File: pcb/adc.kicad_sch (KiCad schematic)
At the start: 19 parts, among them U2 PCM1802DB, X1 ECS-2520MVLC-081.92

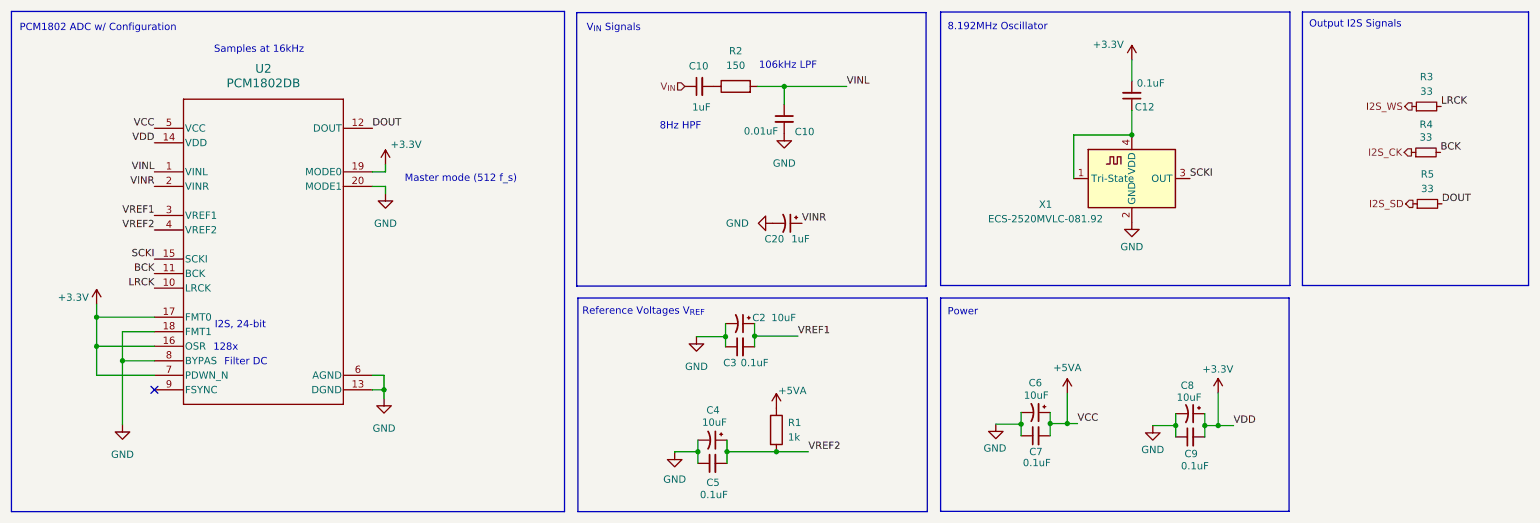
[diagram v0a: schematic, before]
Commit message: Reordered components
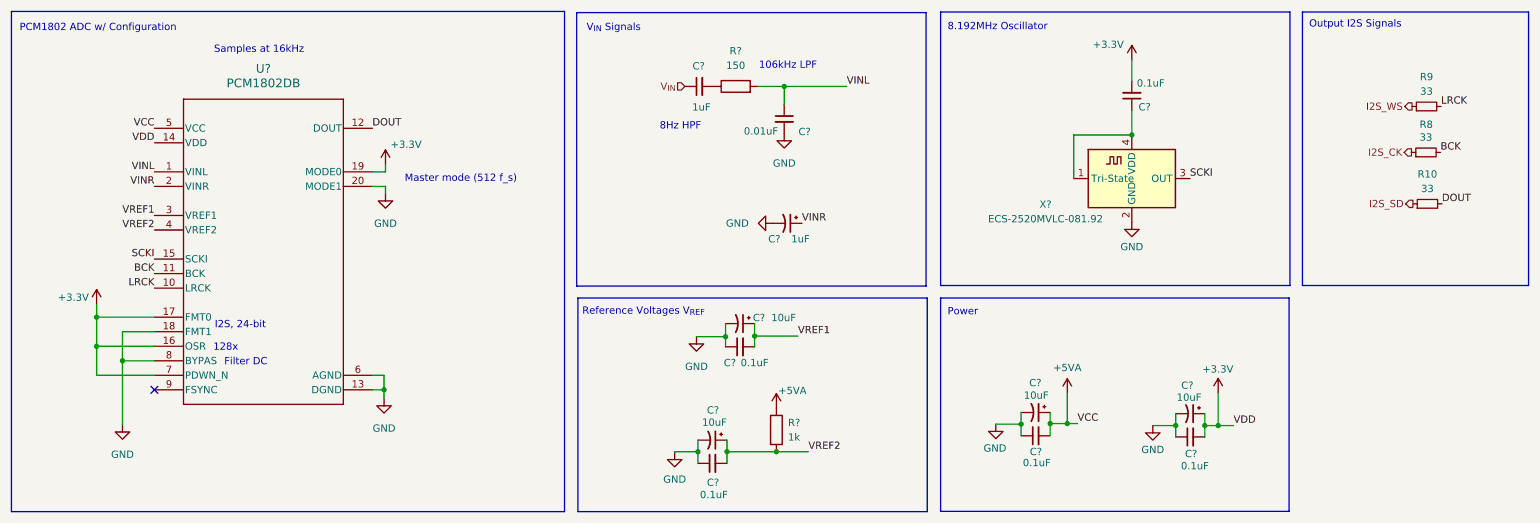
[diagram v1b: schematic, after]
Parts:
- renumbered C5 to C?, C4 to C?, C7 to C?, C3 to C?, C9 to C?, C6 to C?, C10 to C?, C2 to C?, C20 to C?, C8 to C?, C12 to C?, R5 to R10, R4 to R8, R3 to R9, R2 to R?, R1 to R?, U2 to U?, X1 to X?

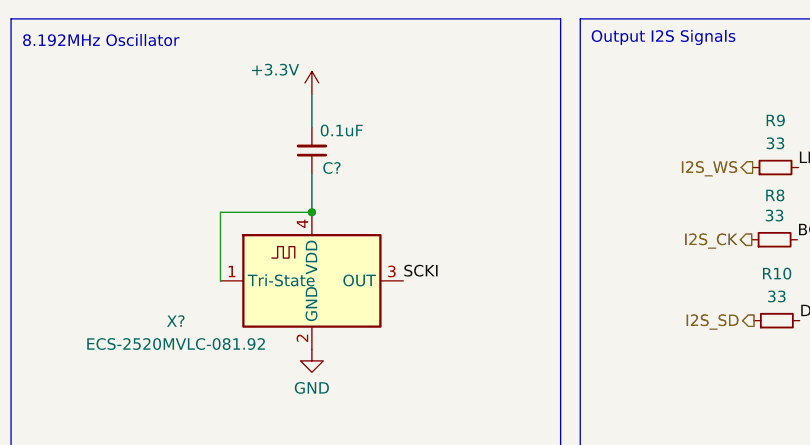
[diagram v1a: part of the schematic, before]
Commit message: Connected VDD cap to GND
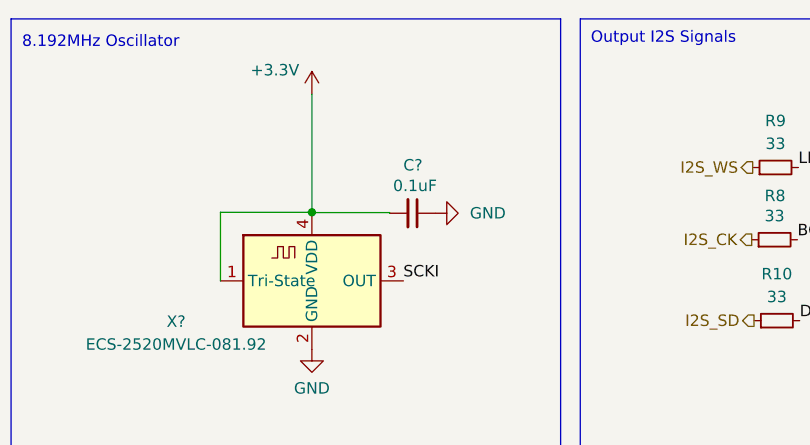
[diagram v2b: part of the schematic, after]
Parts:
- removed C?: 0.1uF, symbol Device:C_Small
- added C?: 0.1uF, symbol Device:C_Small
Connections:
- net +3.3V: now also X?.1 (Tri-State), X?.4 (VDD), C?.2
- net GND: now also C?.1
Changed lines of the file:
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@@
+    (stroke (width 0) (type default))
+  )
+  (wire (pts (xy 211.7598 74.4028) (xy 211.7598 74.3712))
+    (stroke (width 0) (type default))
+  )
+  (wire (pts (xy 211.7598 74.4028) (xy 220.3958 74.4028))
     (stroke (width 0) (type default))
   )
@@
     (stroke (width 0) (type default))
   )
-  (wire (pts (xy 211.7598 70.0532) (xy 211.7598 74.3712))
-    (stroke (width 0) (type default))
-  )
   (wire (pts (xy 145.8214 107.3404) (xy 145.8214 109.5248))
     (stroke (width 0) (type default))
@@
     (stroke (width 0) (type default))
   )
+  (wire (pts (xy 220.3958 74.4028) (xy 220.3958 74.4728))
+    (stroke (width 0) (type default))
+  )
   (wire (pts (xy 30.8102 106.2228) (xy 30.8102 111.3028))
     (stroke (width 0) (type default))
@@
     (stroke (width 0) (type default))
   )
-  (wire (pts (xy 211.7598 61.2648) (xy 211.7598 64.9732))
+  (wire (pts (xy 211.7598 61.2648) (xy 211.7598 74.3712))
     (stroke (width 0) (type default))
   )
@@
     )
   )
+  (symbol (lib_id "power:GND") (at 225.4758 74.4728 90) (unit 1)
+    (in_bom yes) (on_board yes) (dnp no) (fields_autoplaced)
+    (property "Reference" "#PWR080" (at 231.8258 74.4728 0)
+      (effects (font (size 1.27 1.27)) hide)
+    )
+    (property "Value" "GND" (at 229.3112 74.4728 90)
+      (effects (font (size 1.27 1.27)) (justify right))
+    )
+    (property "Footprint" "" (at 225.4758 74.4728 0)
+      (effects (font (size 1.27 1.27)) hide)
+    )
+    (property "Datasheet" "" (at 225.4758 74.4728 0)
+      (effects (font (size 1.27 1.27)) hide)
+    )
+    (pin "1")
+    (instances
+      (project "tuner_pedal"
+        (path "/be09f3cc-c79c-49de-93a4-4a01bf6bfbcf/910ce163-1837-409b-9a8d-6a7a7eac3527"
+          (reference "#PWR080") (unit 1)
+        )
+      )
+    )
+  )
+  (symbol (lib_id "Device:C_Small") (at 222.9358 74.4728 270) (unit 1)
+    (in_bom yes) (on_board yes) (dnp no)
+    (property "Reference" "C?" (at 222.9866 69.1388 90)
+      (effects (font (size 1.27 1.27)))
+    )
+    (property "Value" "0.1uF" (at 223.2152 71.4248 90)
+      (effects (font (size 1.27 1.27)))
+    )
+    (property "Footprint" "" (at 222.9358 74.4728 0)
+      (effects (font (size 1.27 1.27)) hide)
+    )
+    (property "Datasheet" "~" (at 222.9358 74.4728 0)
+      (effects (font (size 1.27 1.27)) hide)
+    )
+    (pin "1")
+    (pin "2")
+    (instances
+      (project "tuner_pedal"
+        (path "/be09f3cc-c79c-49de-93a4-4a01bf6bfbcf"
+          (reference "C?") (unit 1)
+        )
+        (path "/be09f3cc-c79c-49de-93a4-4a01bf6bfbcf/910ce163-1837-409b-9a8d-6a7a7eac3527"
+          (reference "C19") (unit 1)
+        )
+      )
+    )
+  )
   (symbol (lib_id "power:+5VA") (at 149.6314 122.1232 0) (unit 1)
     (in_bom yes) (on_board yes) (dnp no)
@@
         )
       )
-    )
-  )
-  (symbol (lib_id "Device:C_Small") (at 211.7598 67.5132 180) (unit 1)
-    (in_bom yes) (on_board yes) (dnp no)
-    (property "Reference" "C?" (at 213.995 69.4944 0)
-      (effects (font (size 1.27 1.27)))
-    )
-    (property "Value" "0.1uF" (at 215.0618 65.3288 0)
-      (effects (font (size 1.27 1.27)))
-    )
-    (property "Footprint" "" (at 211.7598 67.5132 0)
-      (effects (font (size 1.27 1.27)) hide)
-    )
-    (property "Datasheet" "~" (at 211.7598 67.5132 0)
-      (effects (font (size 1.27 1.27)) hide)
-    )
-    (pin "1")
-    (pin "2")
-    (instances
-      (project "tuner_pedal"
-        (path "/be09f3cc-c79c-49de-93a4-4a01bf6bfbcf"
-          (reference "C?") (unit 1)
-        )
-        (path "/be09f3cc-c79c-49de-93a4-4a01bf6bfbcf/910ce163-1837-409b-9a8d-6a7a7eac3527"
-          (reference "C19") (unit 1)
-        )
-      )
